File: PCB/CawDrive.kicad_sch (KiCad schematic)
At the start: 64 parts, among them CN2 WAFER-SH1.0-6PWB, CN3 WAFER-SH1.0-4PWB, U1 TJA1051T/3/1J, U10 WAFER-SH1.0-2PWB, U11 WAFER-SH1.0-2PWB, U12 WAFER-SH1.0-2PWB, U5 WAFER-SH1.0-2PWB, U6 WAFER-SH1.0-2PWB, U8 STM32F446RETx, U9 MT6835GT-STD, X1 CSTNE16M0V530000R0

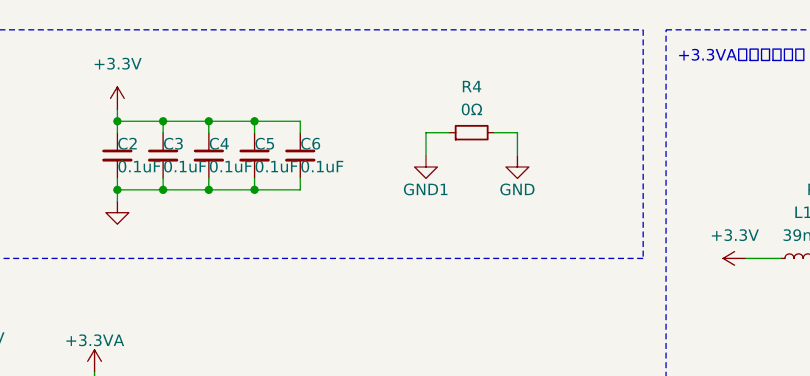
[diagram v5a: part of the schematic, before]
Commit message: 优化ADC采样布线
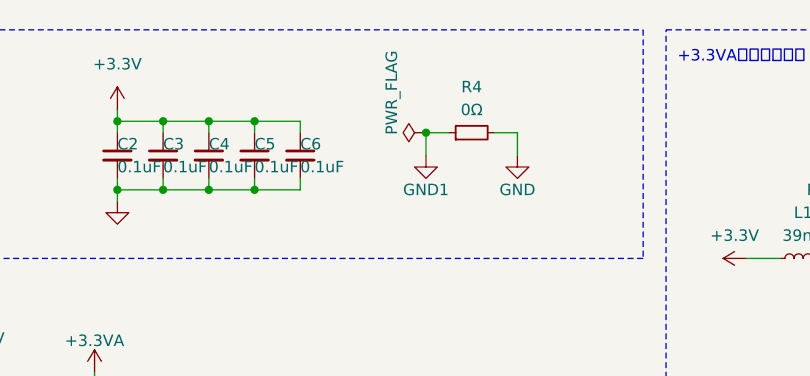
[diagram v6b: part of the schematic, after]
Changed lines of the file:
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@@
 	)
 	(junction
+		(at 102.87 24.13)
+		(diameter 0)
+		(color 0 0 0 0)
+	)
+	(junction
 		(at 157.48 86.36)
 		(diameter 0)
@@
 					(unit 1)
 				)
+			)
+		)
+	)
+	(symbol
+		(lib_id "power:PWR_FLAG")
+		(at 102.87 24.13 90)
+		(unit 1)
+		(exclude_from_sim no)
+		(in_bom yes)
+		(on_board yes)
+		(dnp no)
+		(property "Reference" "#FLG09"
+			(at 100.965 24.13 0)
+			(effects
+				(font
+					(size 1.27 1.27)
+				)
+				(hide yes)
+			)
+		)
+		(property "Value" "PWR_FLAG"
+			(at 99.06 19.685 0)
+			(effects
+				(font
+					(size 1.27 1.27)
+				)
+			)
+		)
+		(property "Footprint" ""
+			(at 102.87 24.13 0)
+			(effects
+				(font
+					(size 1.27 1.27)
+				)
+				(hide yes)
+			)
+		)
+		(property "Datasheet" "~"
+			(at 102.87 24.13 0)
+			(effects
+				(font
+					(size 1.27 1.27)
+				)
+				(hide yes)
+			)
+		)
+		(property "Description" "Special symbol for telling ERC where power comes from"
+			(at 102.87 24.13 0)
+			(effects
+				(font
+					(size 1.27 1.27)
+				)
+				(hide yes)
+			)
+		)
+		(pin "1"
+		)
+		(instances
+			(project "CawDrive"
+				(path "/80524a83-b783-469c-b956-da06086e2ffd"
+					(reference "#FLG09")
+					(unit 1)
+				)

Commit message: 优化PCB
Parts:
- removed D5: SMF6.0CA_C2836402, Rick_Diode:SMF6.0CA_SOD-123FL_L2.8-W1.8-LS3.7-BI, symbol Rick_Diode:SMF6.0CA
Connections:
- net ADC3_IN2: now also C12.2, R20.1, R21.2
- removed net ADC3_IN3: C12.2, R20.1, R21.2, U8.17 (PA3)
- no-connect marks 32 -> 33
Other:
- sheet DRV8323RSRGZR ports: added none; removed I_C
